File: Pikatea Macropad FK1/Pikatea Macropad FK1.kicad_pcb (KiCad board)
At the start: 2 copper layers, 125.1 x 22.4 mm, 9 parts, among them J1 Conn_01x12_Female, J2 Conn_01x06_Male, J4 Conn_01x03_Male, SW1 Rotary_Encoder_Switch

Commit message: updates to XL macropad
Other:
- board text added: "https://pikatea.com/guides for instructions."

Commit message: add gerbers2
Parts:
- MX1, MX2, MX3, MX4, MX5: footprint MX_Only:MXOnly-1U -> MX_Only:MXOnly-1U-NoLED

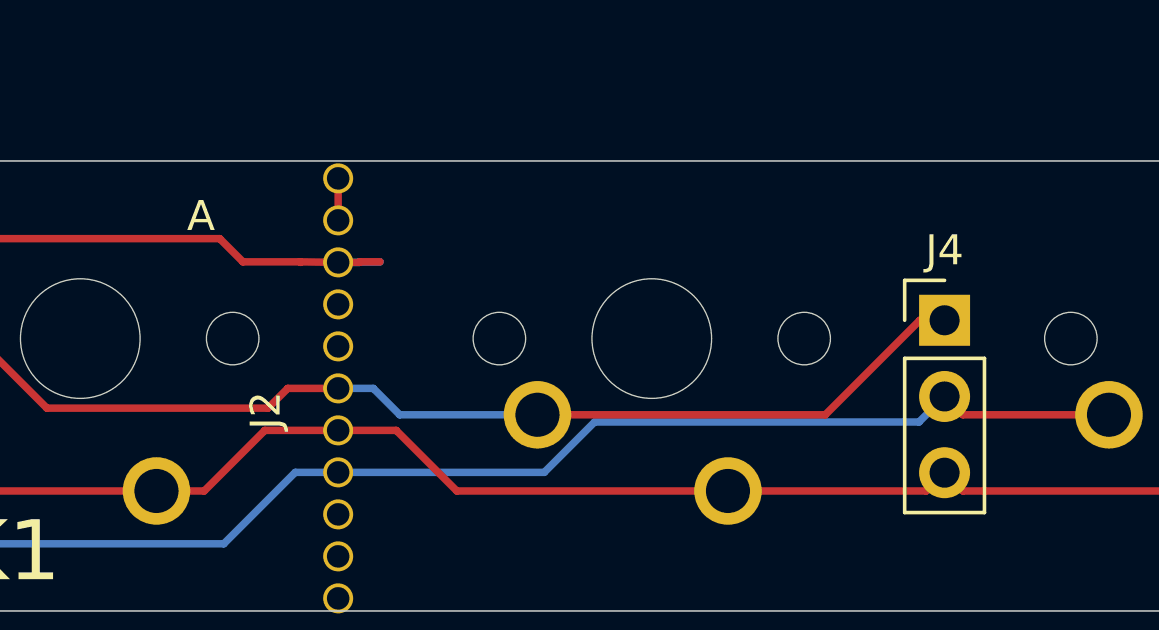
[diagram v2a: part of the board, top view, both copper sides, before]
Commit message: add gerbers flip labels
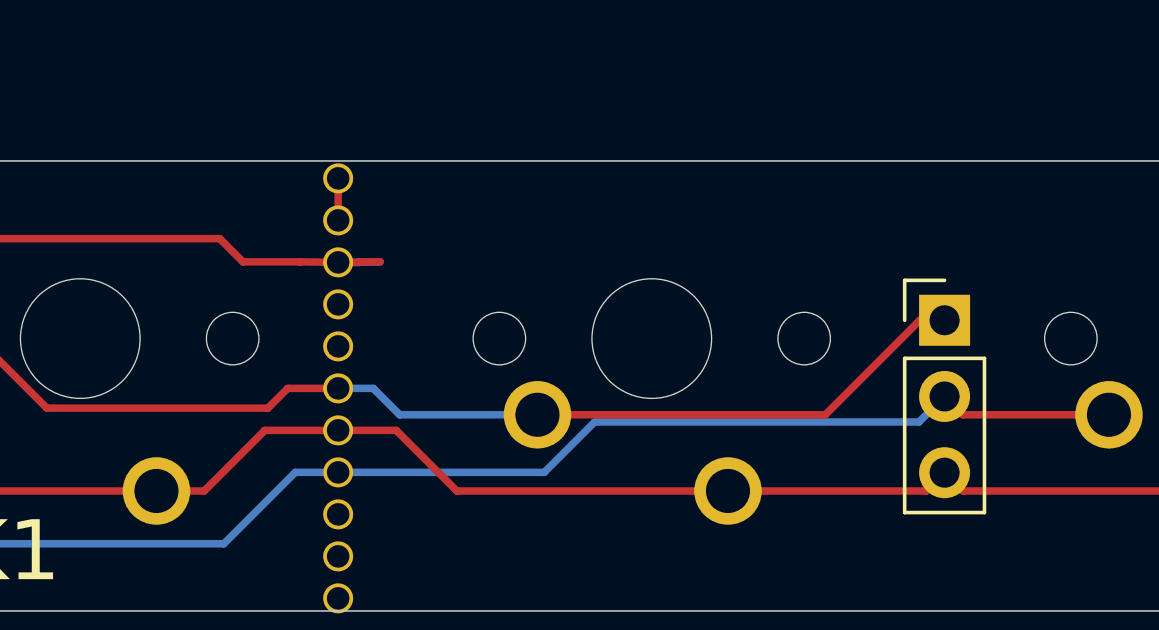
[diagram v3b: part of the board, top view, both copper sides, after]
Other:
- board text removed: "A"
